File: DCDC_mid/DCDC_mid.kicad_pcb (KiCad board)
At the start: 2 copper layers, 148.8 x 49.8 mm, 36 parts, among them J1 Conn_01x02_Pin, J2 Conn_01x02_Pin, Q1 BD139, Q2 BD140, Q4 BD139, Q5 C2M0025120D, U1 LM311, U2 TL431LP

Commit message: DCDC_mit verbessert, hoffentlich
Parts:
- removed the C7 at (143.6, 131.0)
- removed the D4 at (143.6, 115.8)
- removed Q5: C2M0025120D, Package_TO_SOT_THT:TO-247-3_Vertical
- added Q4: Q_PMOS_GDSD, Package_TO_SOT_SMD:TO-263-3_TabPin4, F.Cu at (154.8, 110.4)
- R7: renamed from R5; value 10R -> 1R
- moved D4 11.7 mm to (155.0, 131.0)
- moved D3 11.3 mm to (165.0, 124.4)
- moved R7 11.1 mm to (141.5, 108.8), turned to 90 degrees
- moved C7 8.26 mm to (140.0, 118.0)
- renumbered C6 to C1, C5 to C2, C1 to C3, C9 to C4, C10 to C5, C2 to C6, C8 to C7, C3 to C8, C4 to C9, D2 to D1, D1 to D2, D5 to D3, D3 to D4, Q4 to Q1, Q1 to Q2, Q2 to Q3, R3 to R1, R1 to R3, R7 to R4, R6 to R5, R4 to R6, U2 to U1, U1 to U2
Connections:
- C3 pad 1: Net-(U1--) -> Net-(U1-K)
- C5 pad 2: Net-(U1-+) -> Net-(U2--)
- C7 pad 2: Net-(D4-K) -> +VDC
- Q2 pad 2: Net-(D4-K) -> +VDC
- R1 pad 2: Net-(U1--) -> Net-(U1-K)
- R2 pad 1: Net-(U1--) -> Net-(U1-K)
- R4 pad 1: Net-(U1-+) -> Net-(U2--)
- R6 pad 1: Net-(D4-K) -> +VDC
- U1 pad 3: Net-(U1--) -> Net-(U1-K)
- U2 pad 2: Net-(U1-+) -> Net-(U1-K)
- U2 pad 3: Net-(U1--) -> Net-(U2--)
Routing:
- net +VDC: track 85.1 -> 116.5 mm
- net Net-(D4-K): track 29.1 -> 0.00 mm
- net Net-(U1--): track 23.7 -> 0.00 mm
- net Net-(U1-K): track 0.00 -> 22.5 mm
- net Net-(U1-+): track 12.6 -> 0.00 mm
- net Net-(U2--): track 0.00 -> 12.4 mm
- net Net-(D3-K): track 12.0 -> 0.00 mm, vias 0 -> 12
- net Net-(Q2-E): track 41.9 -> 30.1 mm
- net Net-(J2-Pin_2): track 205.4 -> 197.5 mm
- net GND: track 92.2 -> 90.8 mm, vias 18 -> 19
- net Net-(Q4-G): track 4.50 -> 5.69 mm
- added copper zone on B.Cu, net Net-(D3-K)

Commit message: DCDC_mid überarbeitet
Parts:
- added C10: 100n, Capacitor_SMD:C_0805_2012Metric_Pad1.18x1.45mm_HandSolder, F.Cu at (114.0, 135.0)
- added R8: 13k, Resistor_SMD:R_0805_2012Metric_Pad1.20x1.40mm_HandSolder, F.Cu at (118.0, 136.0)
- moved R4 2.65 mm to (108.0, 136.0)
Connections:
- R4 pad 2: Net-(J2-Pin_2) -> Net-(C10-Pad2)
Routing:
- net Net-(J2-Pin_2): track 197.5 -> 186.3 mm
- net Net-(C10-Pad2): track 0.00 -> 8.05 mm
- net Net-(U2--): track 12.4 -> 15.0 mm

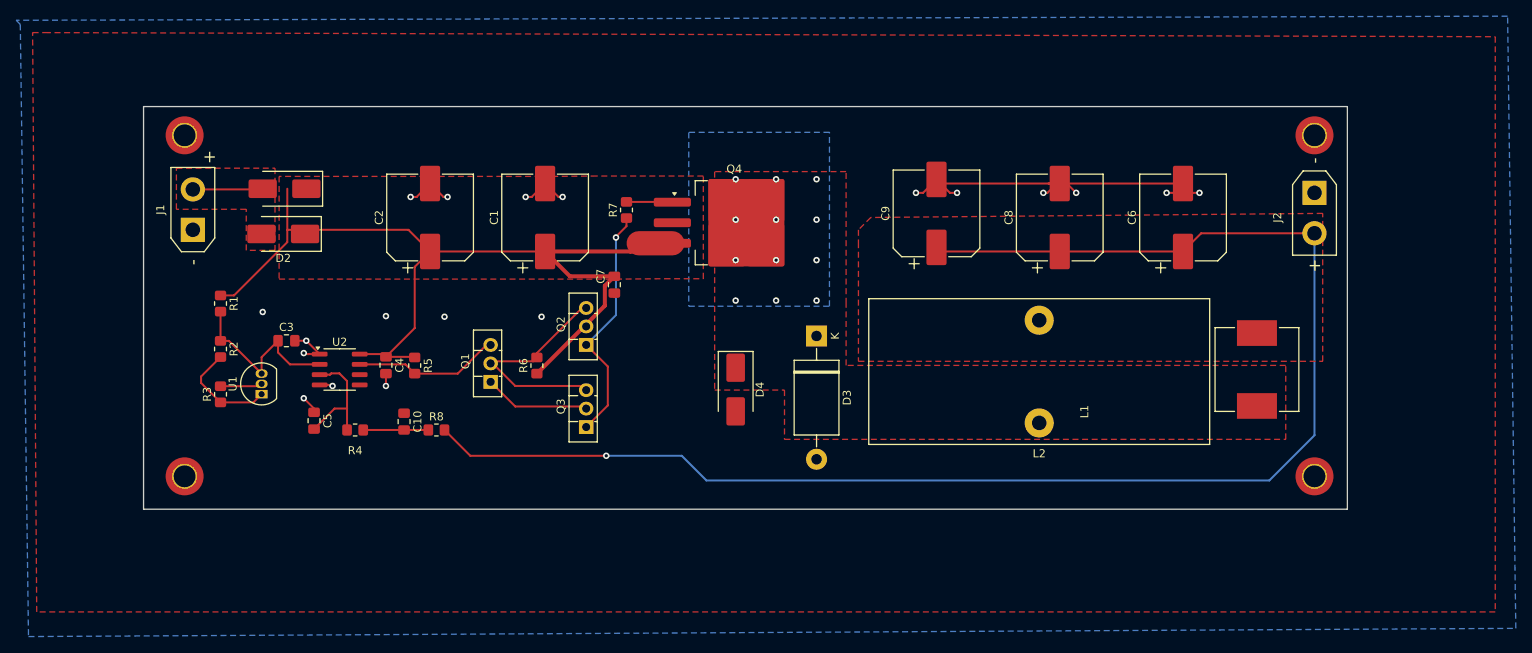
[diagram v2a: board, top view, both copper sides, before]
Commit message: DCDCmid Andere Transistoren
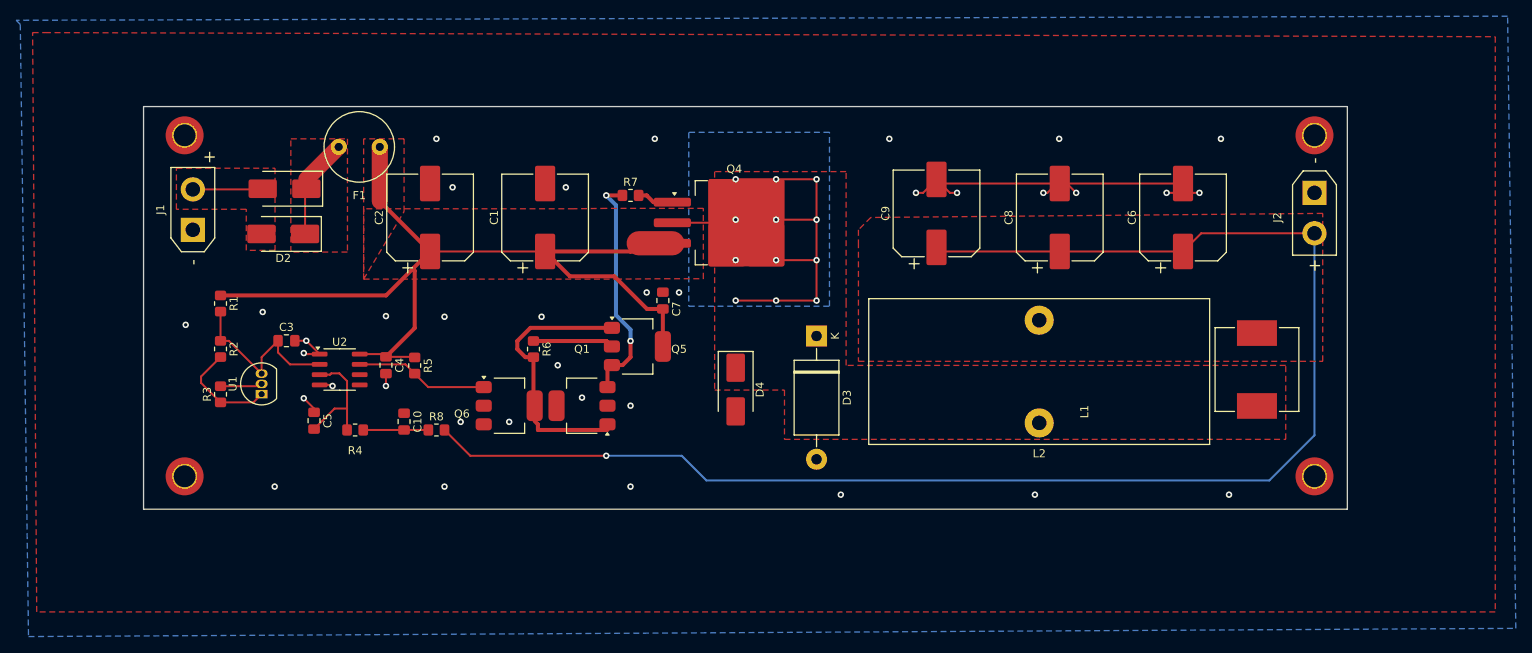
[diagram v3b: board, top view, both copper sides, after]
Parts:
- removed Q2: BD139, Package_TO_SOT_THT:TO-126-3_Vertical
- removed Q3: BD140, Package_TO_SOT_THT:TO-126-3_Vertical
- added F1: Fuse, Fuse:Fuse_Littelfuse_372_D8.50mm, F.Cu at (105.9, 101.0)
- added Q5: FTZ853, Package_TO_SOT_SMD:SOT-223-3_TabPin2, F.Cu at (142.8, 125.7)
- added Q6: FTZ853, Package_TO_SOT_SMD:SOT-223-3_TabPin2, F.Cu at (127.0, 133.0)
- Q1: value BD139 -> FTZ953; footprint Package_TO_SOT_THT:TO-126-3_Vertical -> Package_TO_SOT_SMD:SOT-223-3_TabPin2
- moved Q1 11.7 mm to (136.0, 133.0), turned to 180 degrees
- moved C7 6.31 mm to (146.0, 120.0), turned to -90 degrees
- moved R6 2.08 mm to (130.0, 126.0), turned to -90 degrees
- moved R7 1.87 mm to (142.0, 107.0), turned to 0 degrees
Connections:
- D1 pad 1: +VDC -> Net-(D1-K)
- D2 pad 1: +VDC -> Net-(D1-K)
- Q1 pad 1: GND -> Net-(Q1-B)
- Q1 pad 2: Net-(Q1-C) -> GND
- Q1 pad 3: Net-(Q1-B) -> Net-(Q1-E)
- R5 pad 2: Net-(Q1-B) -> Net-(Q6-B)
- R6 pad 2: Net-(Q1-C) -> Net-(Q1-B)
- R7 pad 1: Net-(Q2-E) -> Net-(Q1-E)
- U2 pad 7: Net-(Q1-B) -> Net-(Q6-B)
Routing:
- net Net-(D3-K): track 0.00 -> 68.0 mm
- net Net-(Q2-E): track 30.1 -> 0.00 mm, vias 1 -> 0
- net Net-(Q1-E): track 0.00 -> 28.9 mm, vias 0 -> 2
- net Net-(Q1-C): track 28.2 -> 0.00 mm
- net GND: track 90.8 -> 63.6 mm, vias 19 -> 36
- net +VDC: track 116.5 -> 141.3 mm
- net Net-(Q6-B): track 0.00 -> 16.5 mm
- net Net-(Q1-B): track 18.3 -> 34.1 mm
- net Net-(D1-K): track 0.00 -> 12.5 mm
- net Net-(Q4-G): track 5.69 -> 4.57 mm
- added copper zone on F.Cu, net Net-(D1-K)

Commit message: Kleinere Änderungen
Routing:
- net Net-(Q1-B): track 34.1 -> 40.4 mm
- net +VDC: track 141.3 -> 147.6 mm
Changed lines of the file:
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@@
 		(tags "CMS SOT")
 		(property "Reference" "Q1"
-			(at 0 7 360)
+			(at 0 7 0)
 			(layer "F.SilkS")
 			(effects
@@
 		)
 		(property "Value" "FTZ953"
-			(at 0 4.5 360)
+			(at 0 4.5 0)
 			(layer "F.Fab")
 			(effects
@@
 		(tags "resistor handsolder")
 		(property "Reference" "R7"
-			(at 0 -1.65 360)
+			(at 0 -1.65 0)
 			(layer "F.SilkS")
 			(effects
@@
 		)
 		(property "Value" "1R"
-			(at 0 1.65 360)
+			(at 0 1.65 0)
 			(layer "F.Fab")
 			(effects
@@
 		)
 		(property "Footprint" "Resistor_SMD:R_0805_2012Metric_Pad1.20x1.40mm_HandSolder"
-			(at 0 0 360)
+			(at 0 0 0)
 			(layer "F.Fab")
 			(hide yes)
@@
 		)
 		(property "Datasheet" ""
-			(at 0 0 360)
+			(at 0 0 0)
 			(layer "F.Fab")
 			(hide yes)
@@
 		)
 		(property "Description" ""
-			(at 0 0 360)
+			(at 0 0 0)
 			(layer "F.Fab")
 			(hide yes)
@@
 		)
 		(fp_text user "${REFERENCE}"
-			(at 0.9 -0.1 360)
+			(at 0.9 -0.1 0)
 			(layer "F.Fab")
 			(effects
@@
 	)
 	(segment
-		(start 139.7 125.675)
-		(end 139.025 125)
-		(width 0.5)
-		(layer "F.Cu")
-		(net 3)
-	)
-	(segment
 		(start 115.241 126.957)
 		(end 115.316 127.032)
@@
 	)
 	(segment
+		(start 139.7 125.675)
+		(end 139.025 125)
+		(width 0.5)
+		(layer "F.Cu")
+		(net 3)
+	)
+	(segment
 		(start 114.539 111.252)
 		(end 117.215 113.928)
@@
 	)
 	(segment
-		(start 130 125)
-		(end 134 125)
-		(width 0.5)
-		(layer "F.Cu")
-		(net 3)
-	)
-	(segment
 		(start 117.215 113.928)
 		(end 131.439 113.928)
@@
 	)
 	(segment
+		(start 139.025 125)
+		(end 130 125)
+		(width 0.5)
+		(layer "F.Cu")
+		(net 3)
+	)
+	(segment
+		(start 139.7 125.675)
+		(end 146 125.675)
+		(width 0.5)
+		(layer "F.Cu")
+		(net 3)
+	)
+	(segment
 		(start 115.316 123.401)
 		(end 111.76 126.957)
@@
 	)
 	(segment
-		(start 139.025 125)
-		(end 134 125)
-		(width 0.5)
-		(layer "F.Cu")
-		(net 3)
-	)
-	(segment
 		(start 143.013 112.915)
 		(end 142 113.928)
@@
 	)
 	(segment
-		(start 139.15 128.525)
-		(end 139.7 127.975)
-		(width 0.25)
+		(start 130.15 133)
+		(end 123.85 133)
+		(width 0.5)
 		(layer "F.Cu")
-		(net 8)
+		(net 7)
 	)
 	(segment
-		(start 141.025 127.975)
-		(end 142 127)
-		(width 0.5)
+		(start 139.15 128.525)
+		(end 139.7 127.975)
+		(width 0.25)
 		(layer "F.Cu")
 		(net 8)
@@
 	(segment
 		(start 142 127)
-		(end 142 125)
+		(end 141.025 127.975)
 		(width 0.5)
 		(layer "F.Cu")
@@
 	)
 	(segment
-		(start 139.7 127.975)
-		(end 141.025 127.975)
+		(start 139.15 130.7)
+		(end 139.15 128.525)
 		(width 0.5)
 		(layer "F.Cu")
@@
 	)
 	(segment
-		(start 139.15 130.7)
-		(end 139.15 128.525)
+		(start 141.025 127.975)
+		(end 139.7 127.975)
 		(width 0.5)
 		(layer "F.Cu")
@@
 	)
 	(via
-		(at 142 125)
+		(at 142 127)
 		(size 0.8)
 		(drill 0.4)
@@
 	)
 	(segment
-		(start 140.2 121.795)
-		(end 140.2 108.2)
+		(start 142 127)
+		(end 142 123.595)
 		(width 0.5)
 		(layer "B.Cu")
@@
 	)
 	(segment
-		(start 142 125)
-		(end 142 123.595)
+		(start 140.2 121.795)
+		(end 140.2 108.2)
 		(width 0.5)
 		(layer "B.Cu")

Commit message: Powerstage2 und HBrücke3 Aufgebaut und verbesserungen eingearbeitet.
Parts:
- R6: value 100 -> 470
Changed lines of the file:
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@@
 			)
 		)
-		(property "Value" "100"
+		(property "Value" "470"
 			(at 0 1.65 90)
 			(layer "F.Fab")
